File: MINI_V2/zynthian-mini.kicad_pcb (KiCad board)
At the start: 2 copper layers, 163 x 120 mm, 90 parts, among them J1 NEUTRIK, SW1 SW_Push, SW10 SW_Push, SW11 SW_Push, SW12 SW_Push, SW13 SW_Push, SW14 SW_Push, SW15 SW_Push, SW16 SW_Push, SW17 SW_Push, SW18 SW_Push, SW19 SW_Push, SW2 SW_Push, SW20 SW_Push, SW3 SW_Push, SW4 SW_Push, SW5 SW_Push, SW6 SW_Push, SW7 SW_Push, SW8 SW_Push, SW9 SW_Push, U1 74HCT14, U2 H11L1M

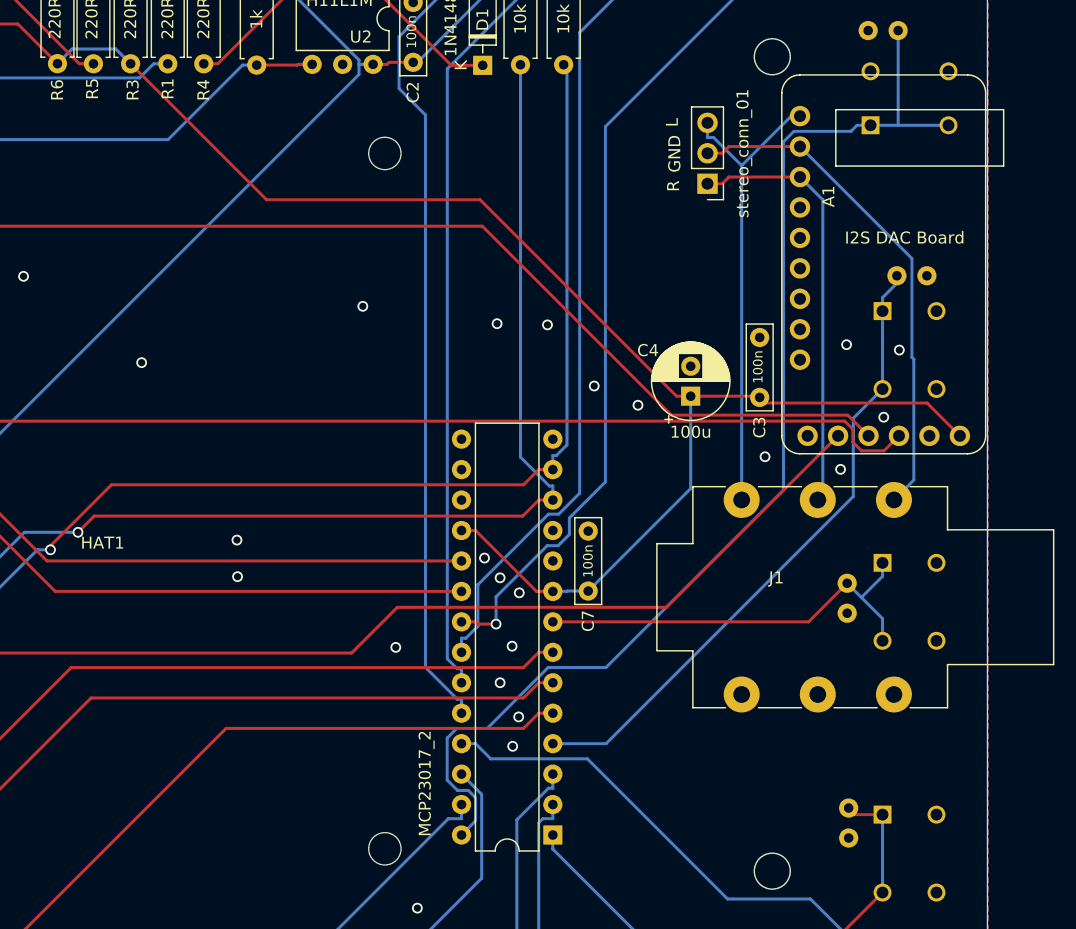
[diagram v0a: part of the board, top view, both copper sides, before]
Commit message: removed PCM sound card, resized pin connector from 3 to 6 pins
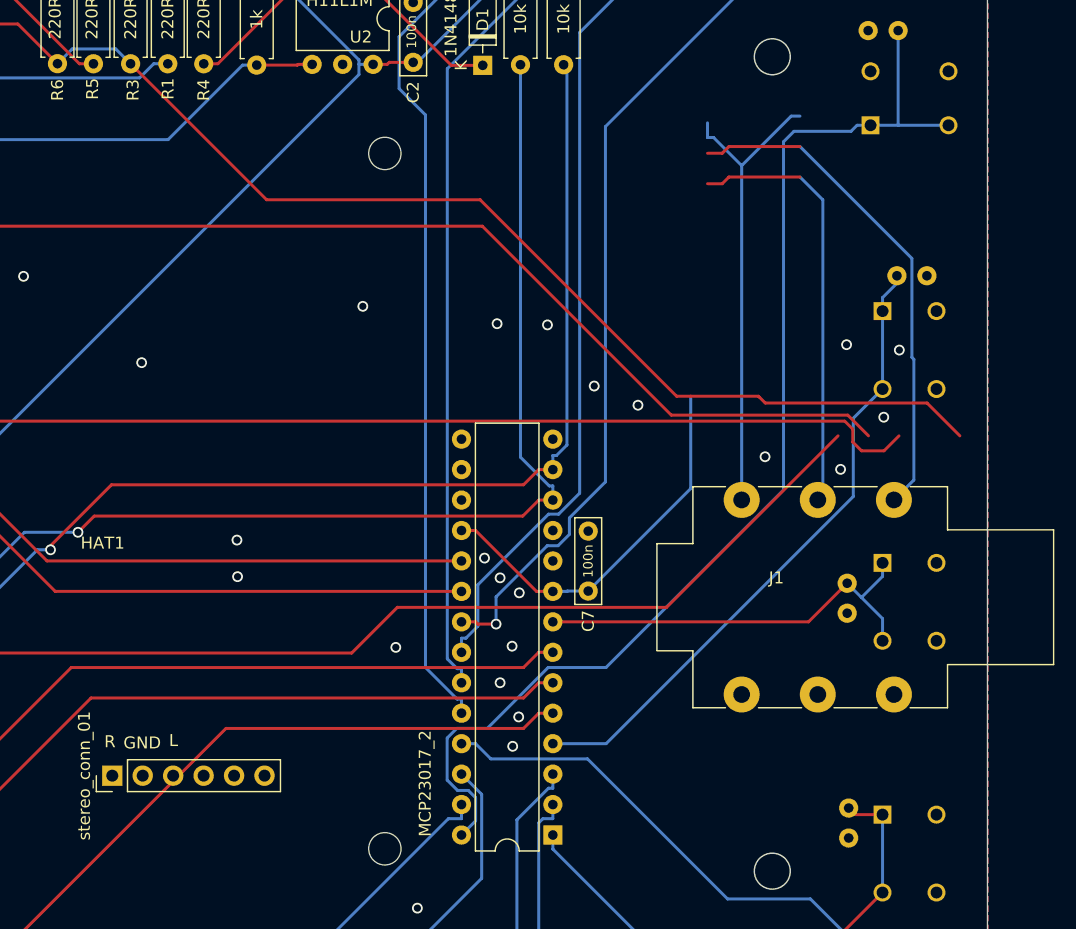
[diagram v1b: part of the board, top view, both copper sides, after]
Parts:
- removed A1: GY-PCM5102, project-footprints:GY-PCM5102
- removed C3: 100n, project-footprints:C_Rect_L7.0mm_W2.0mm_P5.00mm
- removed C4: 100u, Capacitor_THT:CP_Radial_D6.3mm_P2.50mm
- stereo_conn_01: footprint Connector_PinHeader_2.54mm:PinHeader_1x03_P2.54mm_Vertical -> Connector_PinHeader_2.54mm:PinHeader_1x06_P2.54mm_Vertical
- moved stereo_conn_01 70.0 mm to (123.4, 121.4), turned to 90 degrees
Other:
- board text removed: "I2S DAC Board"

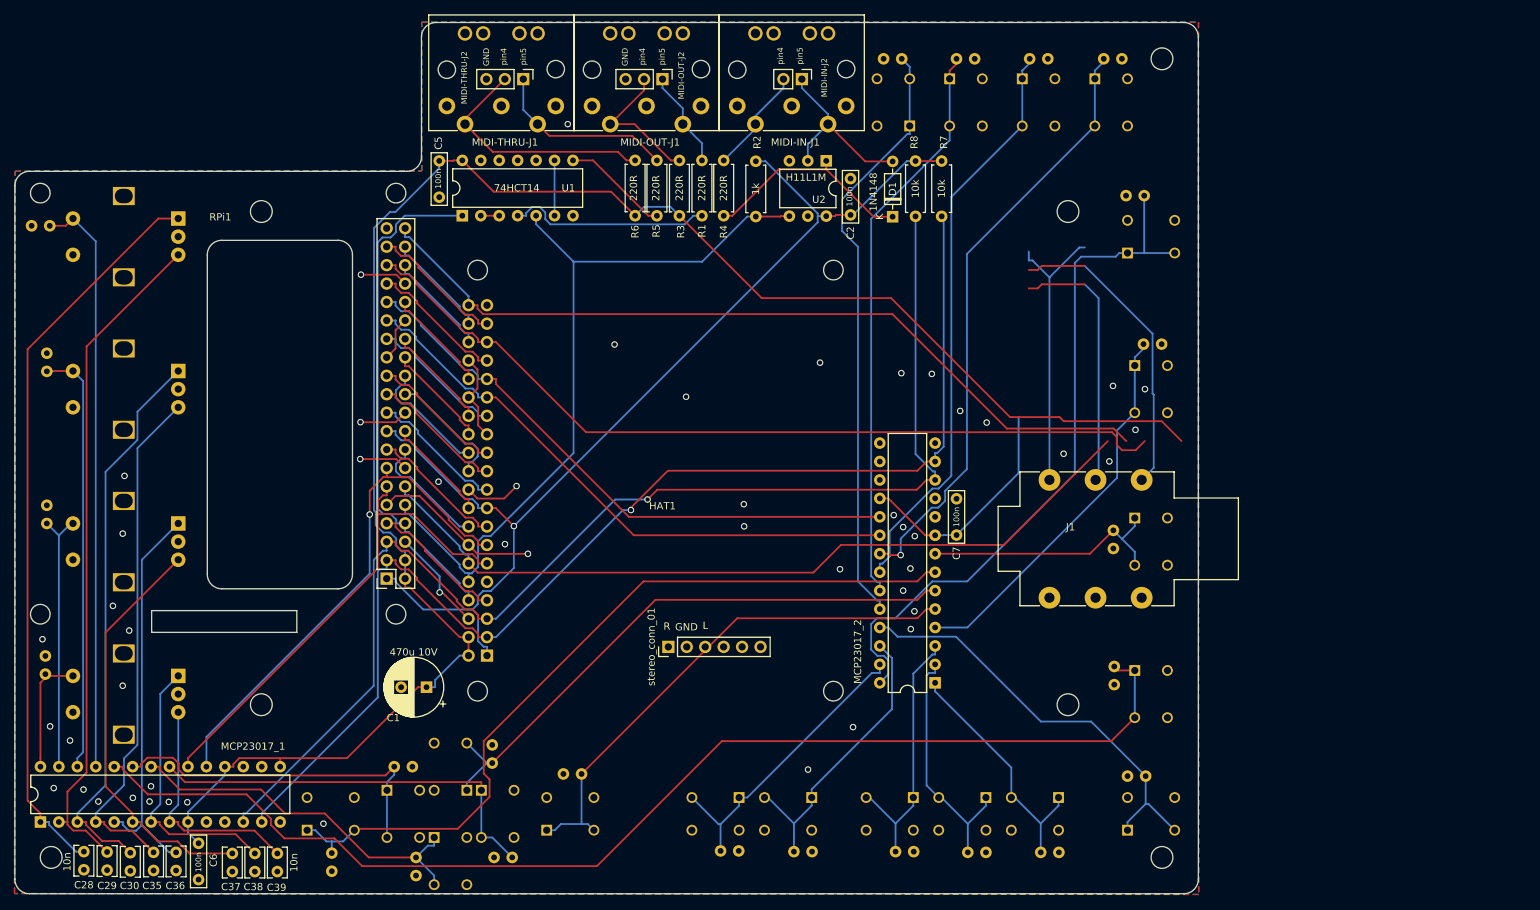
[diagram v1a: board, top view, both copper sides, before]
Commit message: 2x6.3 connectors done, trying one mini jack
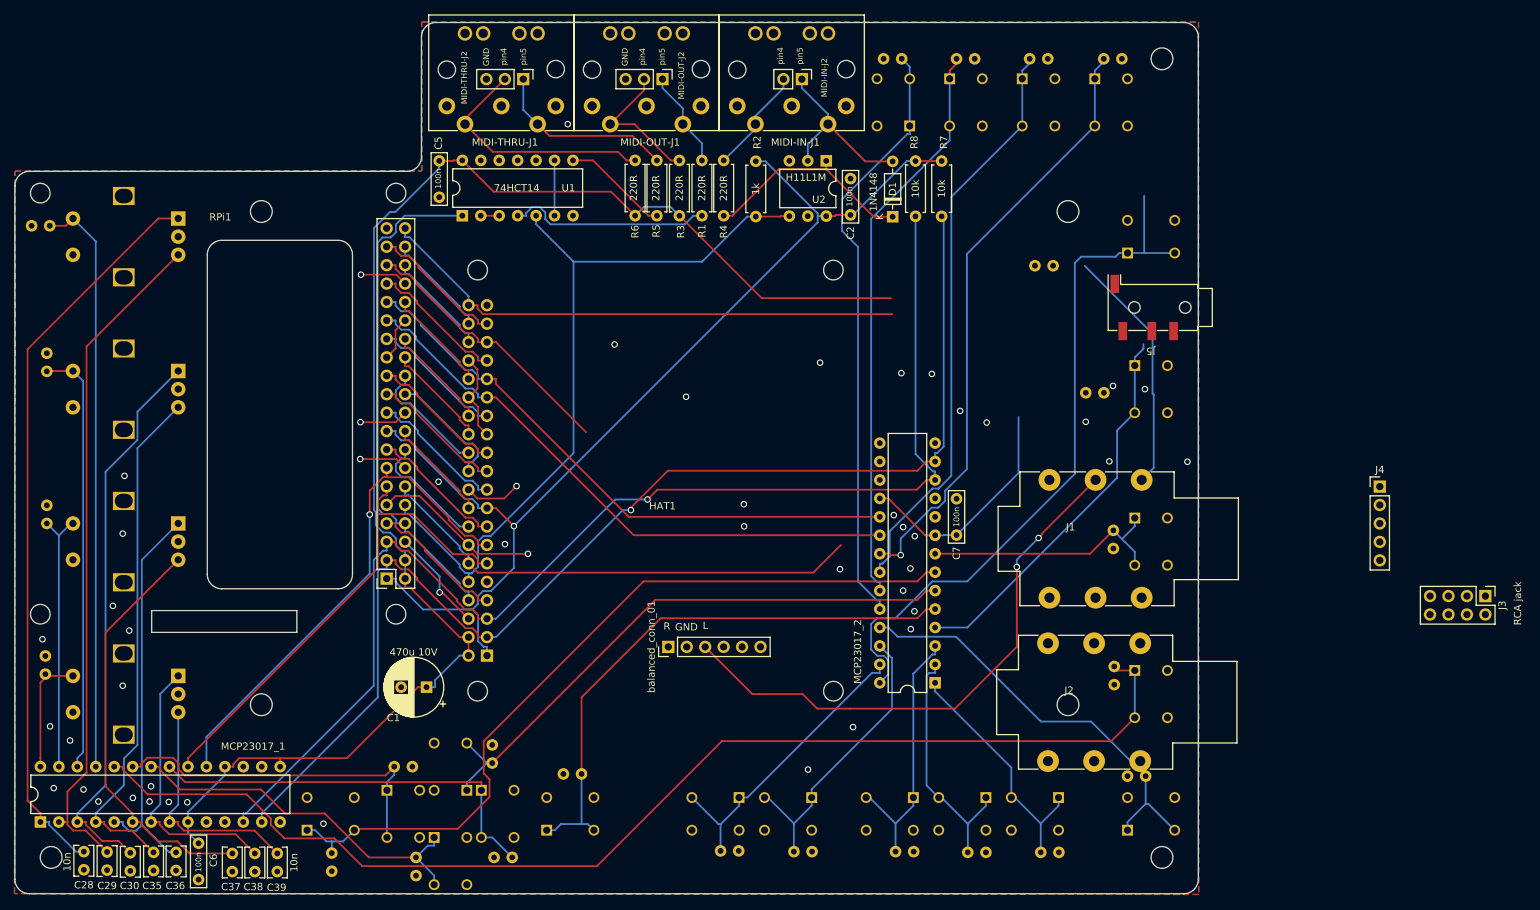
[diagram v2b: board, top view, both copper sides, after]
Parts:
- added J2: NEUTRIK, project-footprints:Jack_6.35mm_Neutrik_NMJ6HFD2_Horizontal, F.Cu at (175.7, 120.9)
- added J3: Conn_02x04_Odd_Even, Connector_PinHeader_2.54mm:PinHeader_2x04_P2.54mm_Vertical, F.Cu at (236.0, 114.4)
- added J4: Conn_01x05, Connector_PinHeader_2.54mm:PinHeader_1x05_P2.54mm_Vertical, F.Cu at (221.4, 99.3)
- added J5: AudioJack3_SwitchT, Connector_Audio:Jack_3.5mm_KoreanHropartsElec_PJ-320D-4A_Horizontal, F.Cu at (189.9, 74.6)
- moved C11 15.8 mm to (176.4, 68.9)
- moved C17 8.64 mm to (183.4, 86.4), turned to 180 degrees
- renumbered stereo_conn_01 to balanced_conn_01
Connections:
- J1 pad R: AUDIO_R_OUT -> AUDIO_L_MINUS
- J1 pad S: AUDIO_GND_OUT -> GND
- J1 pad T: AUDIO_L_OUT -> AUDIO_L_PLUS
- balanced_conn_01 pad 1: AUDIO_R_OUT -> GND
- balanced_conn_01 pad 2: AUDIO_GND_OUT -> AUDIO_L_PLUS
- balanced_conn_01 pad 3: AUDIO_L_OUT -> AUDIO_L_MINUS
- balanced_conn_01 pad 4: (no net) -> GND
- balanced_conn_01 pad 5: (no net) -> AUDIO_R_PLUS
- balanced_conn_01 pad 6: (no net) -> AUDIO_R_MINUS
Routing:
- net I2S_LRCLK: track 116.9 -> 37.7 mm
- net AUDIO_L_MINUS: track 0.00 -> 78.0 mm, vias 0 -> 2
- net +5V: track 286.6 -> 238.4 mm
- net I2S_BCLK: track 110.9 -> 68.2 mm
- net AUDIO_GND_OUT: track 42.0 -> 0.00 mm
- net AUDIO_L_OUT: track 39.5 -> 0.00 mm
- net I2S_AUDIO_OUT_DATA: track 113.2 -> 73.7 mm
- net AUDIO_R_OUT: track 35.8 -> 0.00 mm
- net GND: track 84.0 -> 118.1 mm
- net SWITCH-13: track 72.2 -> 78.4 mm

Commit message: add TRRS jack symbol and footprint, connect to line out
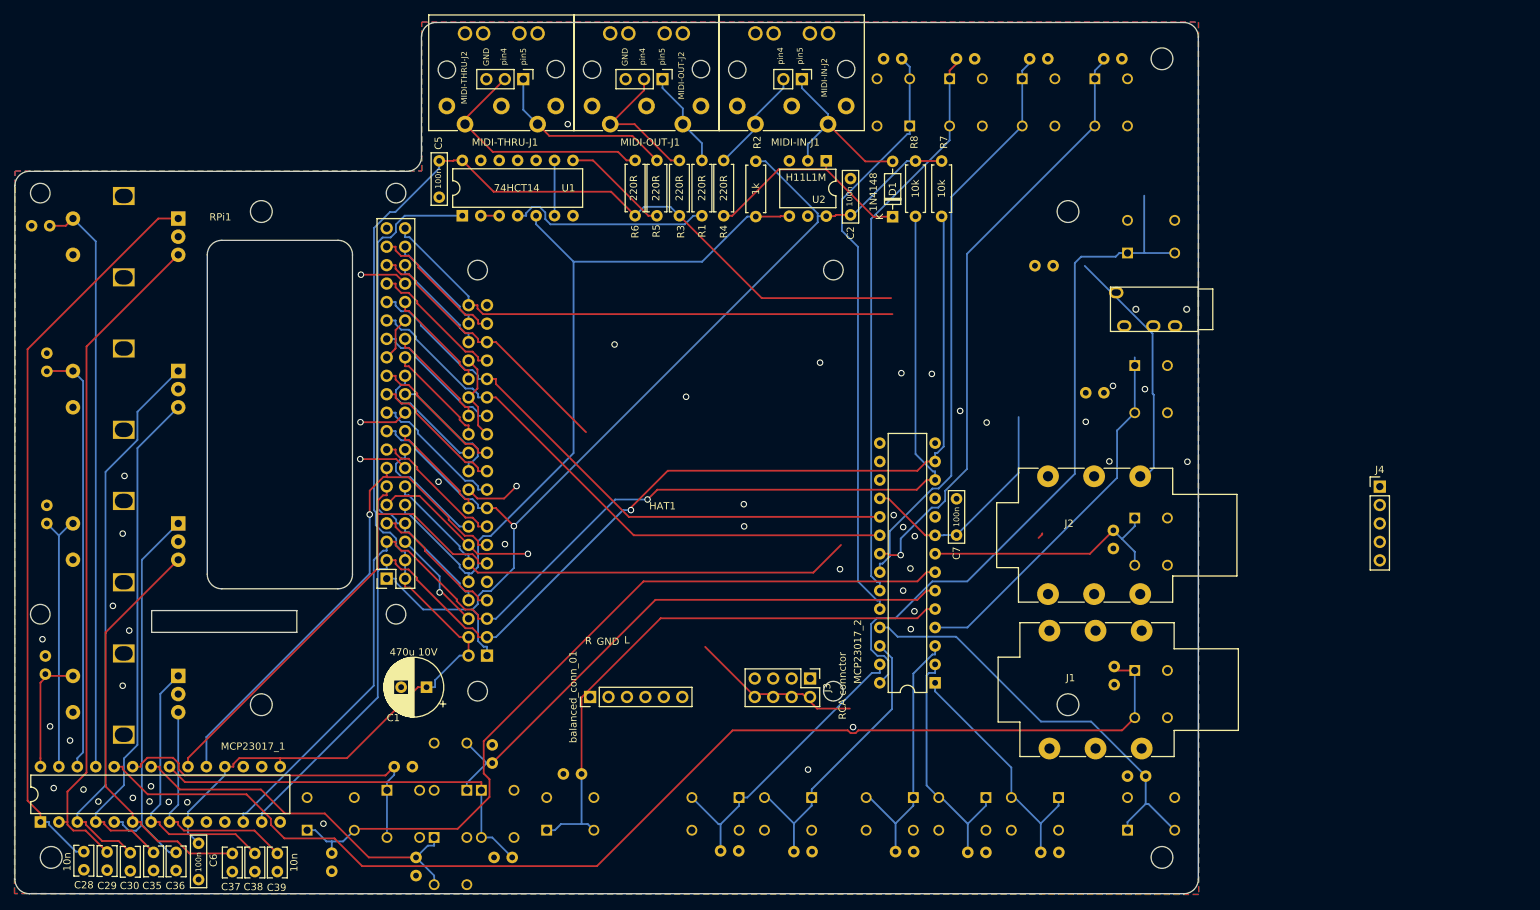
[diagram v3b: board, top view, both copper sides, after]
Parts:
- removed J5: AudioJack3_SwitchT, Connector_Audio:Jack_3.5mm_KoreanHropartsElec_PJ-320D-4A_Horizontal
- added J6: TRRS-PJ-320A, project-footprints:TRRS-PJ-320A, F.Cu at (196.4, 74.9)
- moved J3 93.7 mm to (142.9, 125.7)
- moved J2 23.0 mm to (175.7, 97.9)
- moved J1 20.8 mm to (175.9, 119.1)
- moved balanced_conn_01 12.8 mm to (112.6, 128.3)
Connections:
- J3 pad 2: unconnected-(J3-Pin_2-Pad2) -> GND
- J3 pad 3: unconnected-(J3-Pin_3-Pad3) -> Net-(J3-Pin_3)
- J3 pad 4: unconnected-(J3-Pin_4-Pad4) -> GND
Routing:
- net AUDIO_L_MINUS: track 78.0 -> 24.3 mm, vias 2 -> 0
- net SWITCH-12: track 53.5 -> 51.2 mm
- net AUDIO_R_MINUS: track 0.00 -> 0.59 mm

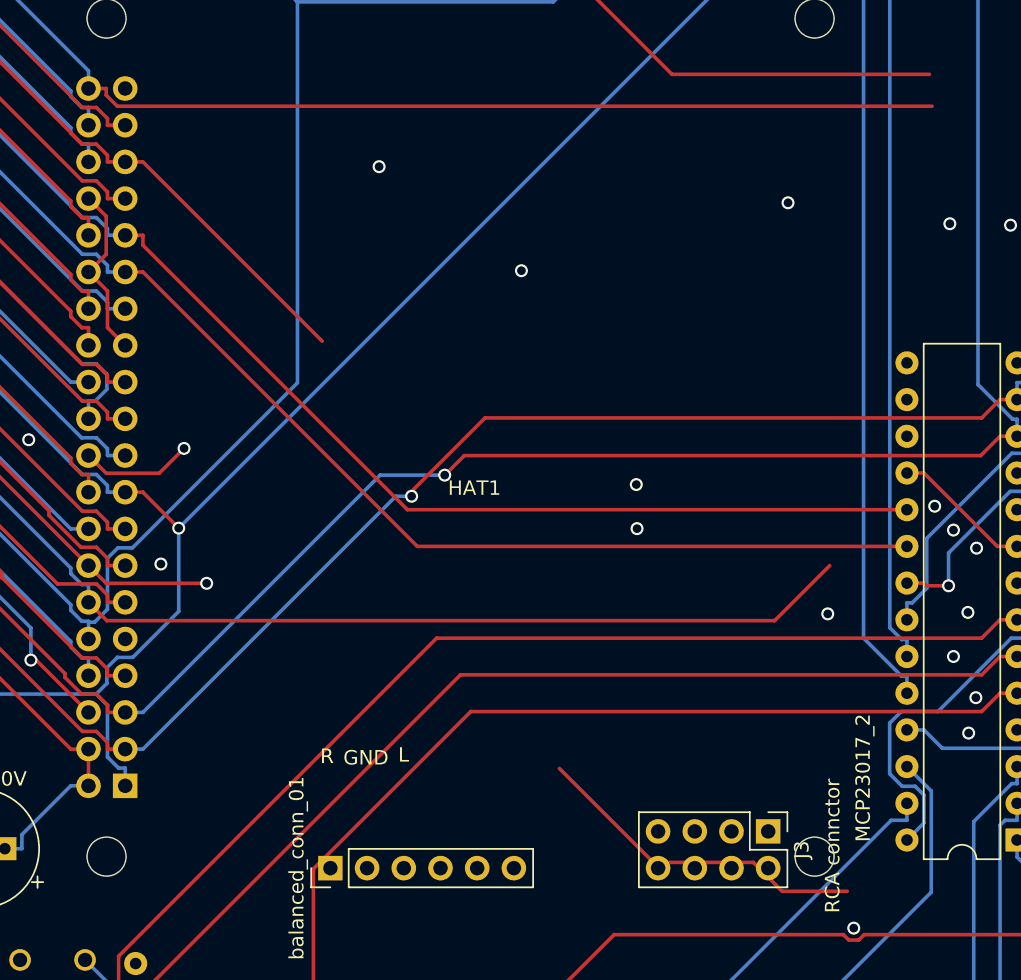
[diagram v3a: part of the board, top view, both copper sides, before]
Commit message: small cleanup for old traces, add 2nd mini jack
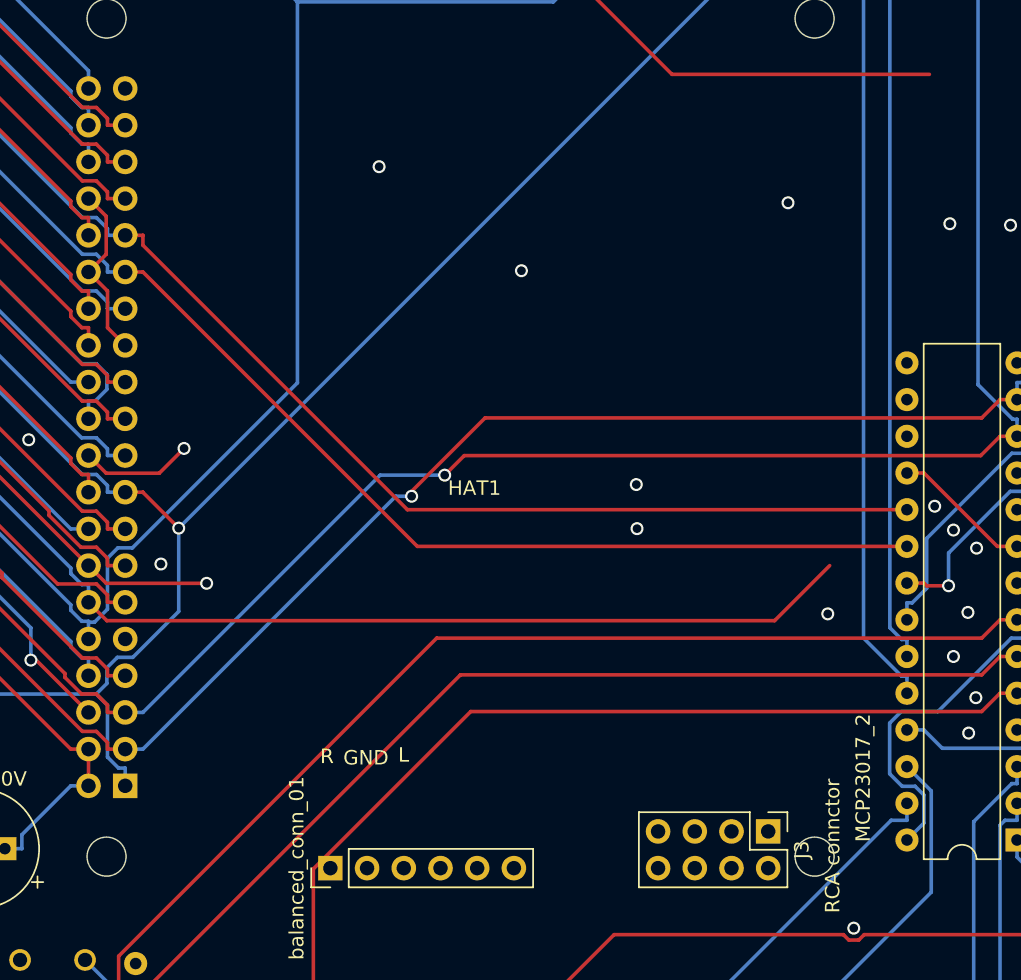
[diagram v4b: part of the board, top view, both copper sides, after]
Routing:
- net I2S_AUDIO_OUT_DATA: track 73.7 -> 14.6 mm
- net AUDIO_L_MINUS: track 24.3 -> 0.86 mm
- net I2S_LRCLK: track 37.7 -> 19.0 mm
- net unconnected-(J3-Pin_8-Pad8): track 0.00 -> 0.92 mm
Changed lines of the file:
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@@
 	)
 	(segment
-		(start 97.1335 74.7737)
-		(end 97.1335 74.3136)
-		(width 0.25)
-		(layer "F.Cu")
-		(net 1)
-	)
-	(segment
-		(start 154.2916 75.5403)
-		(end 97.9001 75.5403)
-		(width 0.25)
-		(layer "F.Cu")
-		(net 1)
-	)
-	(segment
-		(start 95.9068 74.3136)
-		(end 97.1335 74.3136)
-		(width 0.25)
-		(layer "F.Cu")
-		(net 1)
-	)
-	(segment
-		(start 97.9001 75.5403)
-		(end 97.1335 74.7737)
-		(width 0.25)
-		(layer "F.Cu")
-		(net 1)
-	)
-	(segment
 		(start 95.9068 73.0869)
 		(end 87.7602 64.9403)
@@
 	)
 	(segment
-		(start 112.0818 91.8019)
-		(end 99.6735 79.3936)
-		(width 0.25)
-		(layer "F.Cu")
-		(net 18)
-	)
-	(segment
 		(start 96.4535 78.1669)
 		(end 95.4827 78.1669)
@@
 	)
 	(segment
-		(start 98.4468 79.3936)
-		(end 99.6735 79.3936)
-		(width 0.25)
-		(layer "F.Cu")
-		(net 18)
-	)
-	(segment
 		(start 87.6959 70.0636)
 		(end 86.6177 70.0636)
@@
 	)
 	(segment
-		(start 128.4993 121.3736)
-		(end 134.9993 127.8736)
-		(width 0.25)
-		(layer "F.Cu")
-		(net 99)
-	)
-	(segment
-		(start 143.4193 129.3736)
-		(end 143.9193 129.8736)
-		(width 0.25)
-		(layer "F.Cu")
-		(net 99)
-	)
-	(segment
 		(start 174.4193 106.3736)
 		(end 174.9193 105.8736)
@@
 	)
 	(segment
-		(start 141.9193 127.8736)
-		(end 143.4193 129.3736)
-		(width 0.25)
-		(layer "F.Cu")
-		(net 99)
-	)
-	(segment
-		(start 143.9193 129.8736)
-		(end 148.4193 129.8736)
-		(width 0.25)
-		(layer "F.Cu")
-		(net 99)
-	)
-	(segment
 		(start 134.9993 127.8736)
 		(end 135.9193 127.8736)
 		(width 0.25)
 		(layer "F.Cu")
-		(net 99)
-	)
-	(segment
-		(start 135.9193 127.8736)
-		(end 141.9193 127.8736)
-		(width 0.25)
-		(layer "F.Cu")
-		(net 99)
+		(net 103)
 	)
 	(zone
